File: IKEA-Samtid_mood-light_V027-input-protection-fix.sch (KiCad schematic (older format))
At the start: 9 parts, among them P1 POWER, P2 CONN_1, P3 CONN_1, Q1 IRLML6401PbF, Q2 IRLML6401PbF

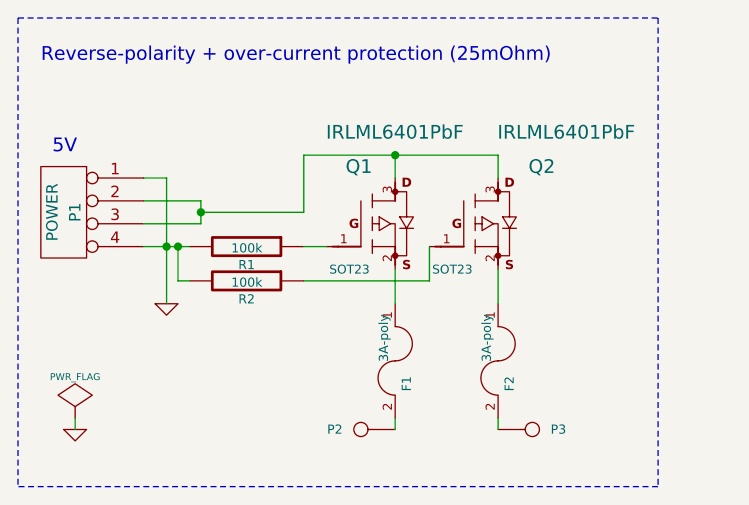
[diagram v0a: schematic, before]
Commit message: One 3A poly-switch is enough: input-protection upgrade board for V0.27 boards.
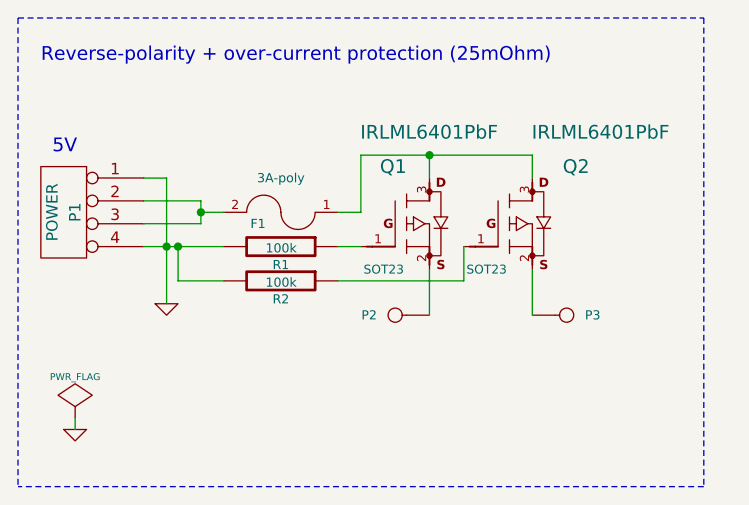
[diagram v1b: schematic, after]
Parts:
- removed F2: 3A-poly, symbol FUSE
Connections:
- net at F1.1: now also Q1.3 (D), Q2.3 (D); no longer Q1.2 (S)
- net at F1.2: now also P1.2 (P2), P1.3 (P3); no longer P2.1
- net at Q2.2 (S): now also P3.1
- new net: P2.1, Q1.2 (S)
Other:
- moved on the sheet: F1, P2, P3, Q1, Q2, R1, R2
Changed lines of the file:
@@
 EESchema Schematic File Version 2
 LIBS:my_parts
-LIBS:atmel
 LIBS:power
 LIBS:device
@@
 LIBS:siliconi
 LIBS:opto
+LIBS:atmel
 LIBS:contrib
 LIBS:valves
-LIBS:IKEA-Samtid_mood-light-cache
 EELAYER 24 0
 EELAYER END
@@
 Sheet 1 1
 Title "IKEA-Samtid_mood-light_V027-input-protection-fix"
-Date "24 Aug 2014"
-Rev "0.1"
+Date "25 Aug 2014"
+Rev "0.2"
 Comp "2014 - blog.spitzenpfeil.org"
 Comment1 ""
@@
 L FUSE F1
 U 1 1 53C3478B
-P 2300 2150
-F 0 "F1" H 2400 2200 40  0000 C CNN
-F 1 "3A-poly" H 2200 2100 40  0000 C CNN
-F 2 "" H 2300 2150 60  0000 C CNN
-F 3 "" H 2300 2150 60  0000 C CNN
-	1    2300 2150
-	0    1    1    0
-$EndComp
-$Comp
-L FUSE F2
-U 1 1 53C34893
-P 2750 2150
-F 0 "F2" H 2850 2200 40  0000 C CNN
-F 1 "3A-poly" H 2650 2100 40  0000 C CNN
-F 2 "" H 2750 2150 60  0000 C CNN
-F 3 "" H 2750 2150 60  0000 C CNN
-	1    2750 2150
-	0    1    1    0
+P 1800 1500
+F 0 "F1" H 1900 1550 40  0000 C CNN
+F 1 "3A-poly" H 1800 1350 40  0000 C CNN
+F 2 "" H 1800 1500 60  0000 C CNN
+F 3 "" H 1800 1500 60  0000 C CNN
+	1    1800 1500
+	-1   0    0    1
 $EndComp
 Text Notes 800  1250 0    60   ~ 0
@@
 	1200 1350 1300 1350
 Wire Wire Line
-	1200 1650 1400 1650
+	1200 1650 1550 1650
 Wire Wire Line
 	1450 1550 1200 1550
@@
 	1300 1350 1300 1900
 Connection ~ 1300 1650
-Wire Wire Line
-	1450 1500 1900 1500
 Connection ~ 1450 1500
 Wire Wire Line
@@
 L MOSFET_P Q1
 U 1 1 53FA015D
-P 2000 1650
-F 0 "Q1" H 2200 2000 60  0000 R CNN
-F 1 "IRLML6401PbF" H 2600 2150 60  0000 R CNN
-F 2 "SOT23" H 2100 1550 39  0000 C CNN
-F 3 "" H 2000 1650 60  0000 C CNN
-	1    2000 1650
+P 2150 1650
+F 0 "Q1" H 2350 2000 60  0000 R CNN
+F 1 "IRLML6401PbF" H 2750 2150 60  0000 R CNN
+F 2 "SOT23" H 2250 1550 39  0000 C CNN
+F 3 "" H 2150 1650 60  0000 C CNN
+	1    2150 1650
 	1    0    0    -1
 $EndComp
@@
 L MOSFET_P Q2
 U 1 1 53FA1783
-P 2450 1650
-F 0 "Q2" H 3000 2000 60  0000 R CNN
-F 1 "IRLML6401PbF" H 3350 2150 60  0000 R CNN
-F 2 "SOT23" H 2550 1550 39  0000 C CNN
-F 3 "" H 2450 1650 60  0000 C CNN
-	1    2450 1650
-	1    0    0    -1
-$EndComp
-Wire Wire Line
-	2300 1350 2300 1250
-Wire Wire Line
-	2750 1250 2750 1350
-Wire Wire Line
-	2300 1750 2300 1900
-Wire Wire Line
-	1900 1500 1900 1250
-Connection ~ 2300 1250
+P 2600 1650
+F 0 "Q2" H 3150 2000 60  0000 R CNN
+F 1 "IRLML6401PbF" H 3500 2150 60  0000 R CNN
+F 2 "SOT23" H 2700 1550 39  0000 C CNN
+F 3 "" H 2600 1650 60  0000 C CNN
+	1    2600 1650
+	1    0    0    -1
+$EndComp
+Wire Wire Line
+	2450 1350 2450 1250
+Wire Wire Line
+	2900 1250 2900 1350
+Wire Wire Line
+	2450 1750 2450 1950
+Connection ~ 2450 1250
 $Comp
 L R R1
 U 1 1 53FA4260
-P 1650 1650
-F 0 "R1" V 1730 1650 40  0000 C CNN
-F 1 "100k" V 1657 1651 40  0000 C CNN
-F 2 "" V 1580 1650 30  0000 C CNN
-F 3 "" H 1650 1650 30  0000 C CNN
-	1    1650 1650
+P 1800 1650
+F 0 "R1" V 1880 1650 40  0000 C CNN
+F 1 "100k" V 1807 1651 40  0000 C CNN
+F 2 "" V 1730 1650 30  0000 C CNN
+F 3 "" H 1800 1650 30  0000 C CNN
+	1    1800 1650
 	0    1    1    0
 $EndComp
@@
 L R R2
 U 1 1 53FA60FB
-P 1650 1800
-F 0 "R2" V 1730 1800 40  0000 C CNN
-F 1 "100k" V 1657 1801 40  0000 C CNN
-F 2 "" V 1580 1800 30  0000 C CNN
-F 3 "" H 1650 1800 30  0000 C CNN
-	1    1650 1800
+P 1800 1800
+F 0 "R2" V 1880 1800 40  0000 C CNN
+F 1 "100k" V 1807 1801 40  0000 C CNN
+F 2 "" V 1730 1800 30  0000 C CNN
+F 3 "" H 1800 1800 30  0000 C CNN
+	1    1800 1800
 	0    1    1    0
 $EndComp
@@
 	1350 1650 1350 1800
 Wire Wire Line
-	1900 1650 2000 1650
+	2050 1650 2150 1650
 Connection ~ 1350 1650
 Wire Wire Line
-	1350 1800 1400 1800
-Wire Wire Line
-	1900 1250 2750 1250
-Wire Wire Line
-	2450 1650 2450 1800
-Wire Wire Line
-	2450 1800 1900 1800
-Wire Notes Line
-	3450 650  3450 2700
+	1350 1800 1550 1800
+Wire Wire Line
+	2600 1650 2600 1800
+Wire Wire Line
+	2600 1800 2050 1800
 Text Notes 750  850  0    60   ~ 0
 Reverse-polarity + over-current protection (25mOhm)
 Wire Wire Line
-	2750 1750 2750 1900
-Wire Wire Line
-	2300 2400 2300 2450
-Wire Wire Line
-	2750 2450 2750 2400
+	2900 1750 2900 1950
 $Comp
 L GND #PWR01
@@
 	1    0    0    -1
 $EndComp
-Wire Notes Line
-	3450 2700 650  2700
-Wire Notes Line
-	650  650  3450 650
 $Comp
 L CONN_1 P2
 U 1 1 53FA4918
-P 2150 2450
-F 0 "P2" H 2230 2450 40  0000 L CNN
-F 1 "CONN_1" H 2150 2505 30  0001 C CNN
-F 2 "" H 2150 2450 60  0000 C CNN
-F 3 "" H 2150 2450 60  0000 C CNN
-	1    2150 2450
+P 2300 1950
+F 0 "P2" H 2380 1950 40  0000 L CNN
+F 1 "CONN_1" H 2300 2005 30  0001 C CNN
+F 2 "" H 2300 1950 60  0000 C CNN
+F 3 "" H 2300 1950 60  0000 C CNN
+	1    2300 1950
 	-1   0    0    1
 $EndComp
@@
 L CONN_1 P3
 U 1 1 53FA49C7
-P 2900 2450
-F 0 "P3" H 2980 2450 40  0000 L CNN
-F 1 "CONN_1" H 2900 2505 30  0001 C CNN
-F 2 "" H 2900 2450 60  0000 C CNN
-F 3 "" H 2900 2450 60  0000 C CNN
-	1    2900 2450
+P 3050 1950
+F 0 "P3" H 3130 1950 40  0000 L CNN
+F 1 "CONN_1" H 3050 2005 30  0001 C CNN
+F 2 "" H 3050 1950 60  0000 C CNN
+F 3 "" H 3050 1950 60  0000 C CNN
+	1    3050 1950
 	1    0    0    -1
 $EndComp
@@
 Wire Wire Line
 	900  2400 900  2450
+Wire Wire Line
+	2050 1500 2150 1500
+Wire Wire Line
+	2150 1500 2150 1250
+Wire Wire Line
+	2150 1250 2900 1250
+Wire Wire Line
+	1450 1500 1550 1500
+Wire Notes Line
+	650  650  3650 650
+Wire Notes Line
+	3650 650  3650 2700
+Wire Notes Line
+	3650 2700 650  2700
 $EndSCHEMATC
